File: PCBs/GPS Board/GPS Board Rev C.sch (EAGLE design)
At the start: 4 parts

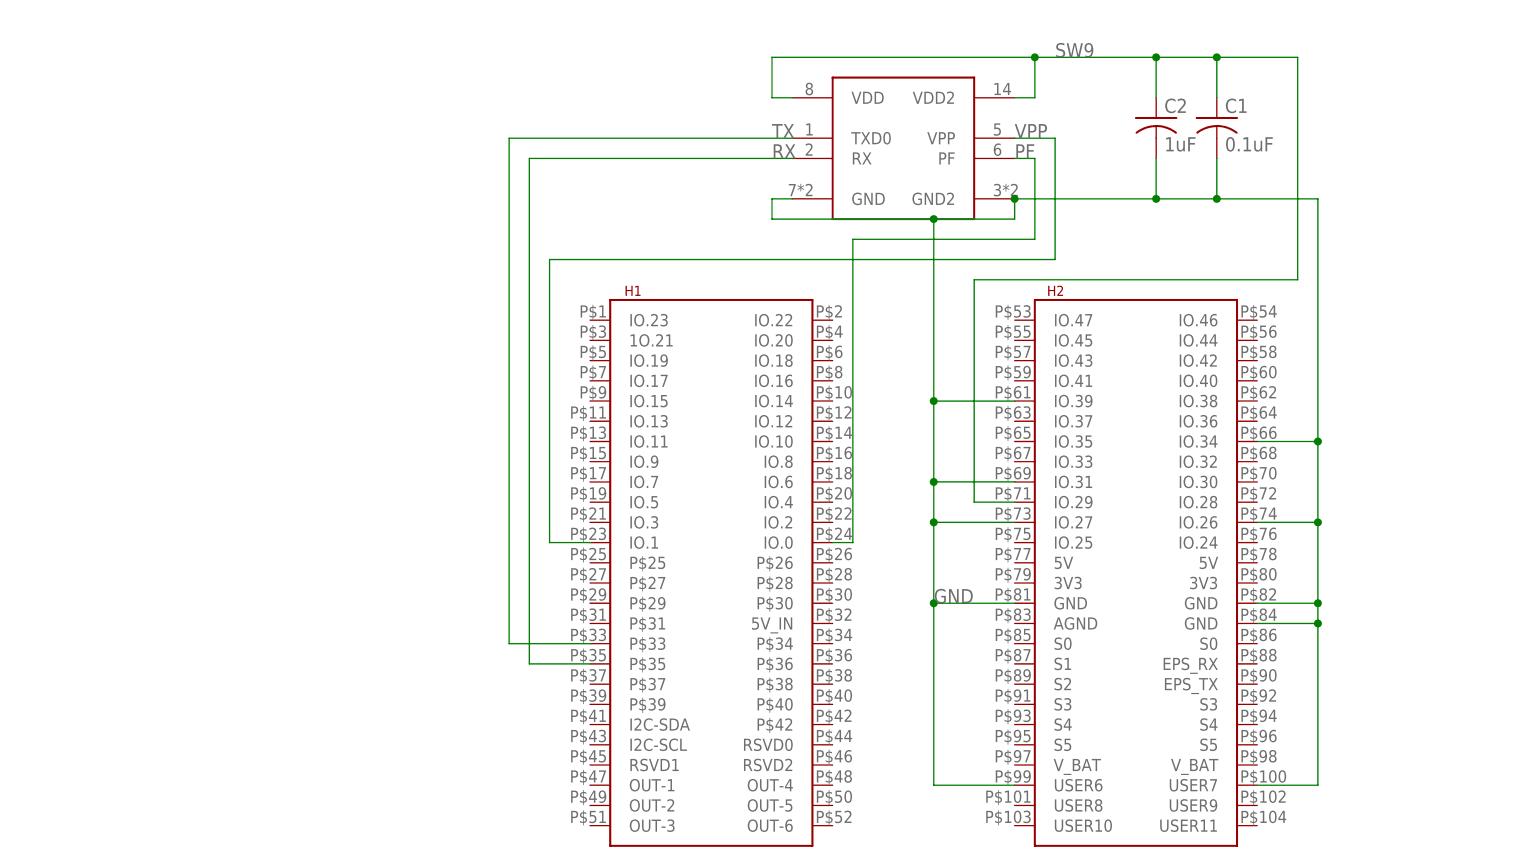
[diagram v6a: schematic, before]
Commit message: Update GPS board to use new library
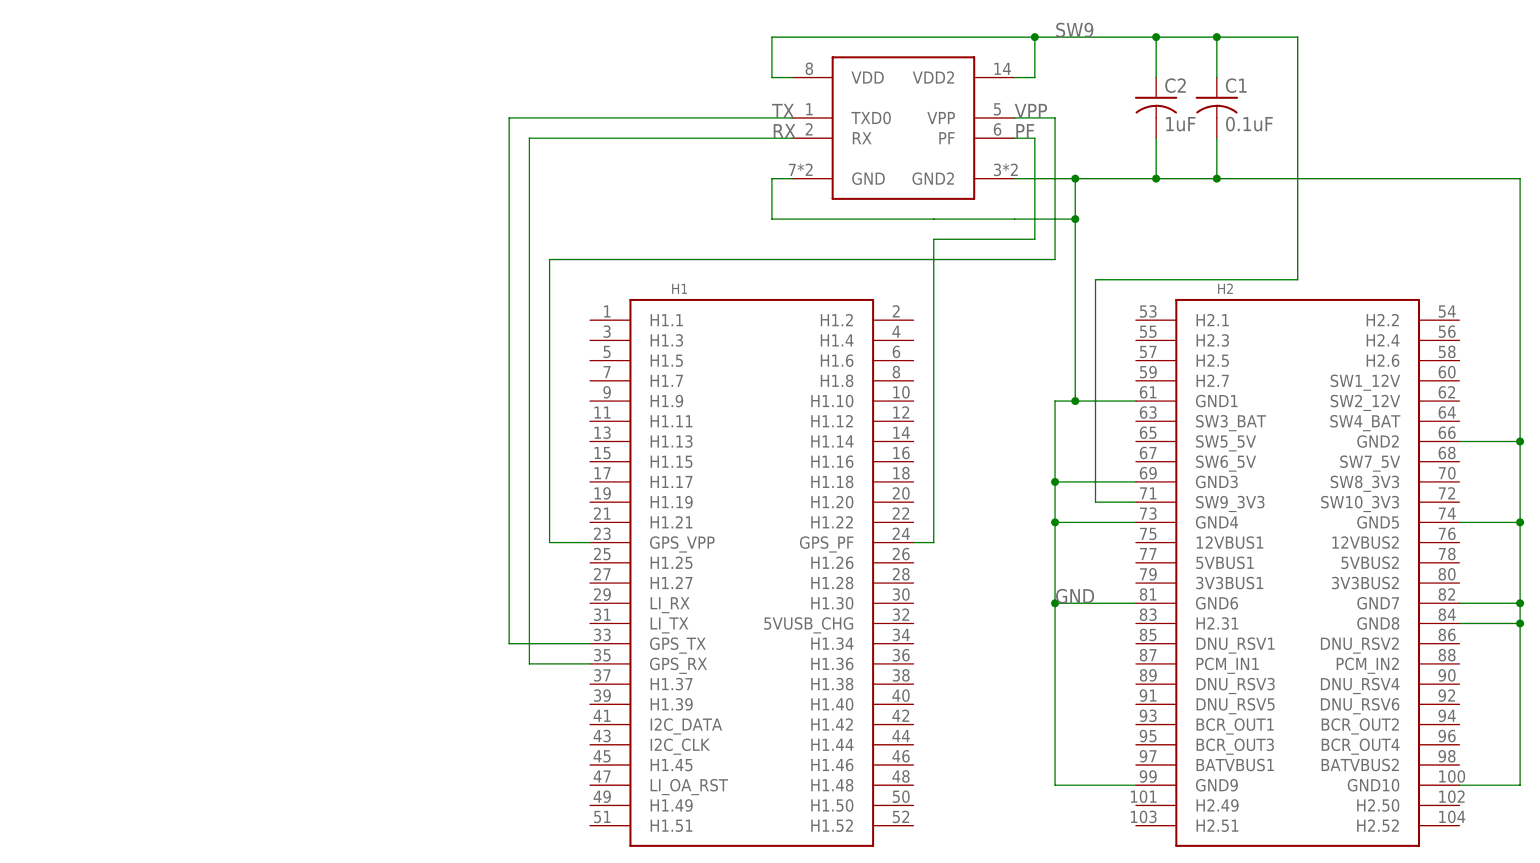
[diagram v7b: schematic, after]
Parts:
- U$1: value PINAVL1 -> PINAV-L1; device pinavl1:PINAVL1 -> Cubesat:PINAV-L1
- U$2: value PC104 -> PC104_GPS; device Cubesat:PC104 -> Cubesat:PC104_GPS
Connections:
- net GND: now also U$2.GND1, U$2.GND10, U$2.GND2, U$2.GND3, U$2.GND4, U$2.GND5, U$2.GND6, U$2.GND7, U$2.GND8, U$2.GND9; no longer U$2.GND@1, U$2.GND@2, U$2.GND@3, U$2.IO.26, U$2.IO.27, U$2.IO.31, U$2.IO.34, U$2.IO.39, U$2.USER6, U$2.USER7
- net PF: now also U$2.GPS_PF; no longer U$2.IO.0
- net RX: now also U$2.GPS_RX; no longer U$2.P$35
- net SW9: now also U$2.SW9_3V3; no longer U$2.IO.29
- net TX: now also U$2.GPS_TX; no longer U$2.P$33
- net VPP: now also U$2.GPS_VPP; no longer U$2.IO.1
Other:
- moved on the sheet: C1, C2

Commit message: Use common PC104 footprint with dimensions set per board
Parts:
- U$2: value PC104_GPS -> PC104_NO_DIMENSION; device Cubesat:PC104_GPS -> Cubesat:PC104_NO_DIMENSION
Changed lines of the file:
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@@
 <part name="C1" library="resistor" library_urn="urn:adsk.eagle:library:348" deviceset="C-US" device="C0805" package3d_urn="urn:adsk.eagle:package:26137/1" value="0.1uF"/>
 <part name="U$1" library="Cubesat" deviceset="PINAV-L1" device=""/>
-<part name="U$2" library="Cubesat" deviceset="PC104_GPS" device=""/>
+<part name="U$2" library="Cubesat" deviceset="PC104_NO_DIMENSION" device=""/>
 </parts>
 <sheets>
